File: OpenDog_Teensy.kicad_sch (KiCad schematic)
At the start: 62 parts

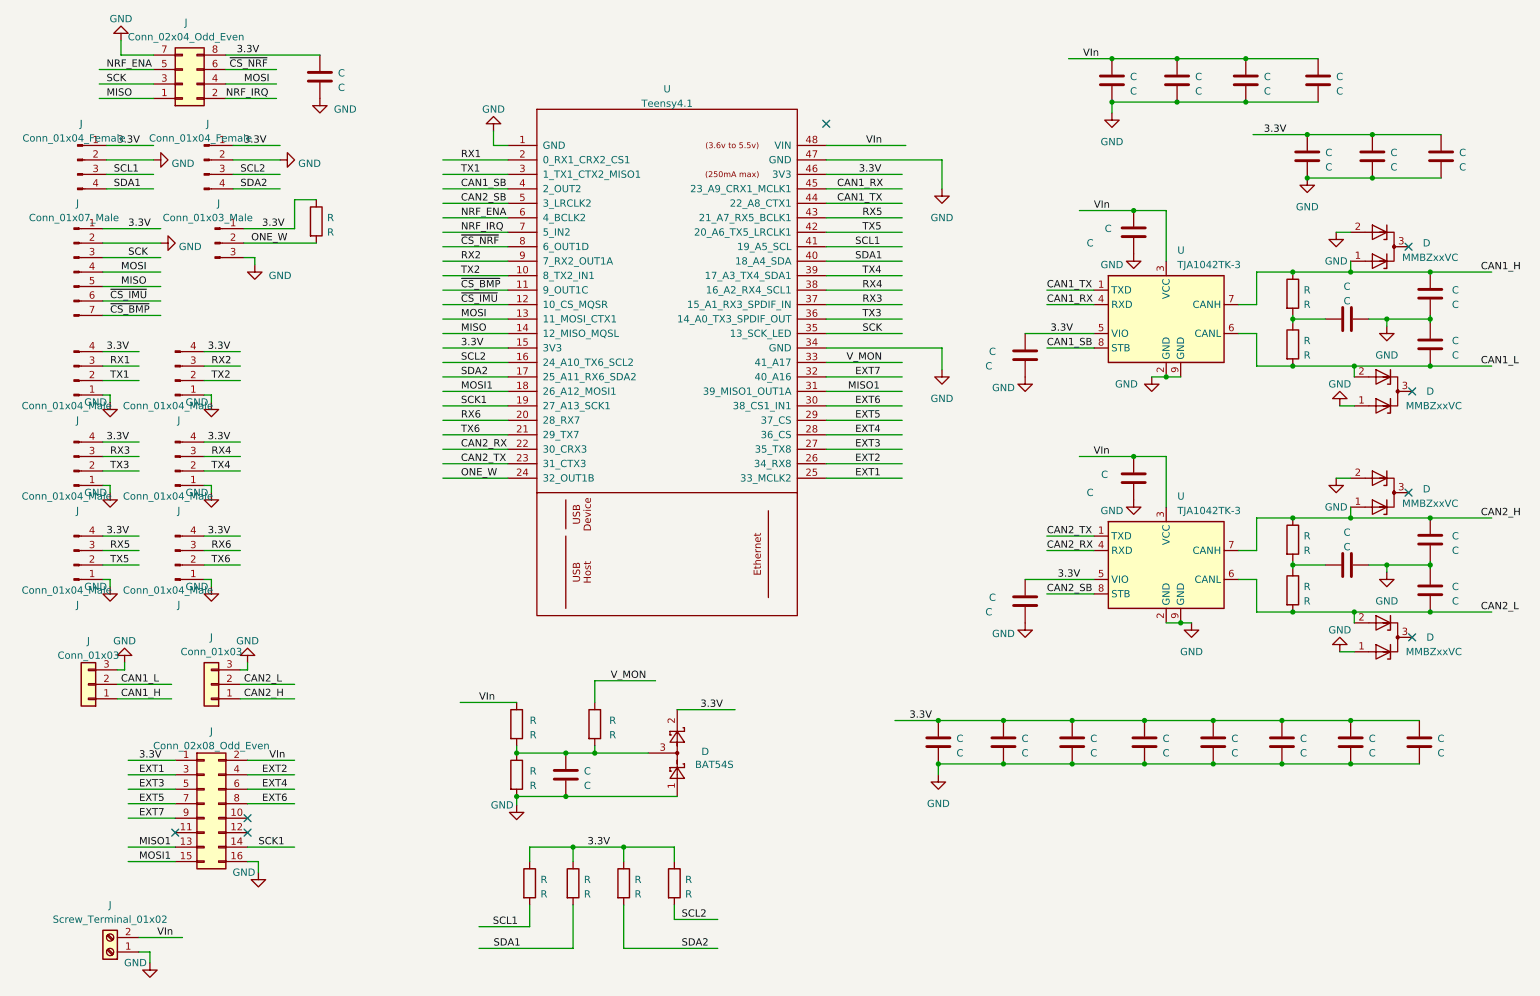
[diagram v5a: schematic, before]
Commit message: OpenDog_Teensy - add buck converter socket. Move the battery monitor to the battery input instead of the 5V input in the old version.
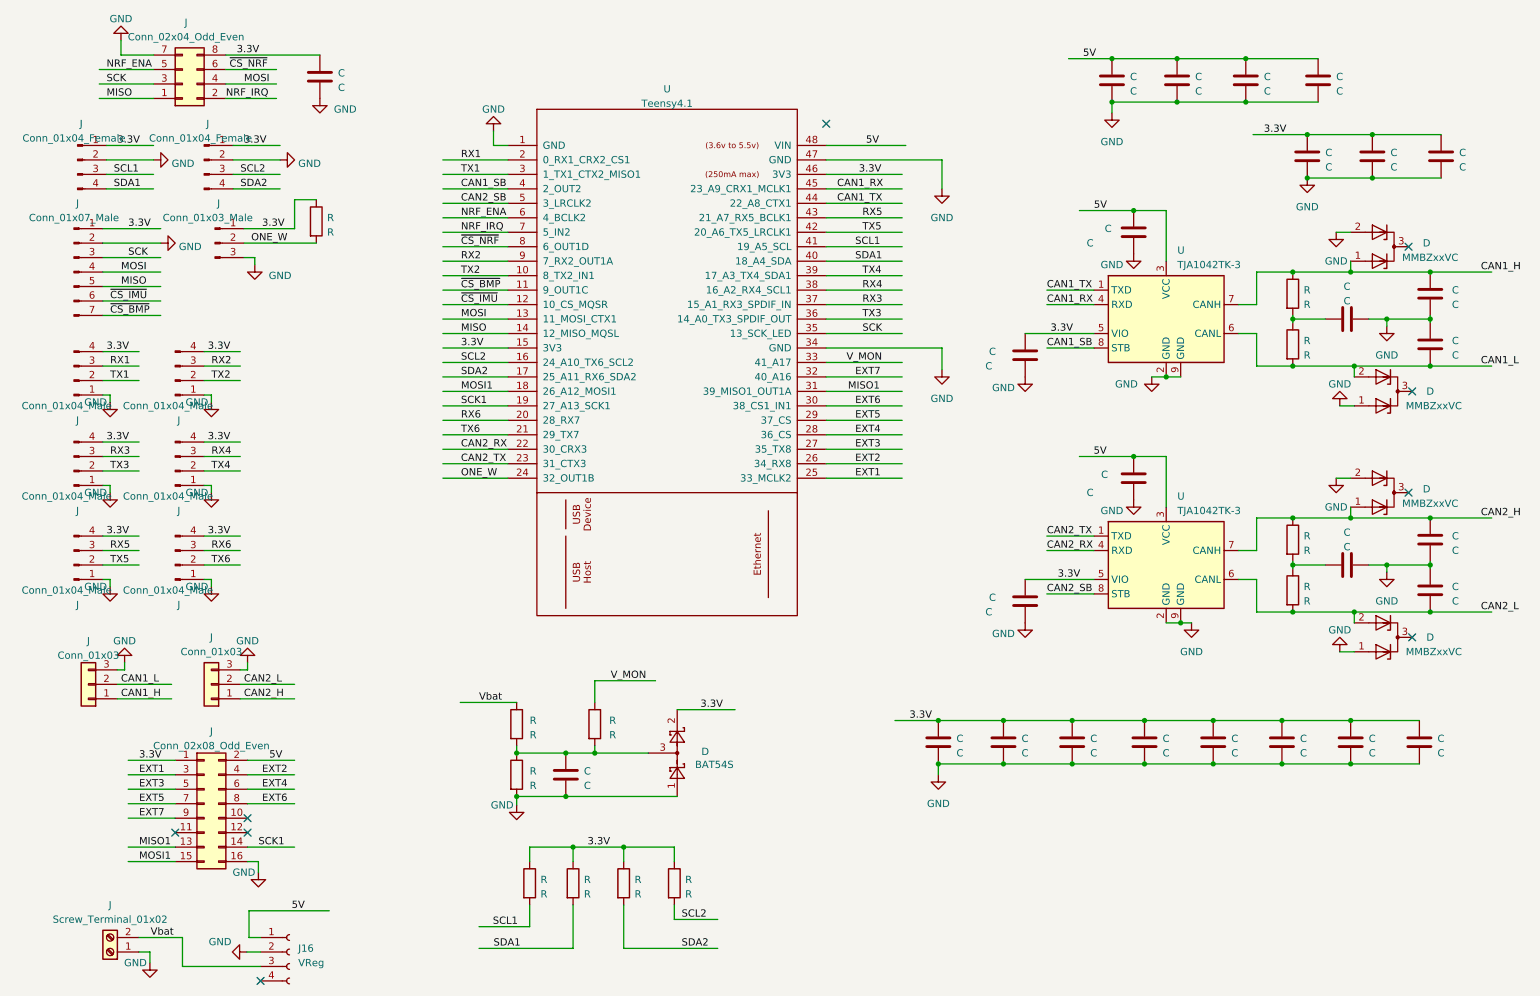
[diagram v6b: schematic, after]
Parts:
- added J16: VReg, Connector_PinSocket_2.54mm:PinSocket_1x04_P2.54mm_Vertical, symbol Connector:Conn_01x04_Female
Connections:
- net GND: now also J16.2 (Pin_2)
- net VIn renamed 5V
- net 5V: now also J16.1 (Pin_1); no longer J.2 (Pin_2), R.1
- new net Vbat: J.2 (Pin_2), J16.3 (Pin_3), R.1
- no-connect marks 8 -> 9
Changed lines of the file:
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@@
-(kicad_sch (version 20220404) (generator eeschema)
+(kicad_sch (version 20220820) (generator eeschema)
   (paper "A4")
   (junction (at 238.125 107.315) (diameter 0) (color 0 0 0 0)
@@
   (no_connect (at 54.61 160.02))
   (no_connect (at 156.21 38.1))
+  (no_connect (at 56.896 188.595))
   (wire (pts (xy 46.99 113.03) (xy 53.34 113.03))
     (stroke (width 0) (type default))
@@
     (stroke (width 0) (type default))
   )
+  (wire (pts (xy 43.18 186.055) (xy 43.18 180.975))
+    (stroke (width 0) (type default))
+  )
   (wire (pts (xy 95.25 182.88) (xy 111.76 182.88))
     (stroke (width 0) (type default))
@@
     (stroke (width 0) (type default))
   )
+  (wire (pts (xy 56.896 180.975) (xy 54.864 180.975))
+    (stroke (width 0) (type default))
+  )
   (wire (pts (xy 50.8 28.575) (xy 59.69 28.575))
     (stroke (width 0) (type default))
@@
     (stroke (width 0) (type default))
   )
+  (wire (pts (xy 56.896 186.055) (xy 43.18 186.055))
+    (stroke (width 0) (type default))
+  )
   (wire (pts (xy 88.9 80.01) (xy 100.33 80.01))
     (stroke (width 0) (type default))
@@
     (stroke (width 0) (type default))
   )
+  (wire (pts (xy 54.864 176.276) (xy 68.961 176.276))
+    (stroke (width 0) (type default))
+  )
   (wire (pts (xy 175.895 150.495) (xy 187.325 150.495))
     (stroke (width 0) (type default))
@@
     (stroke (width 0) (type default))
   )
+  (wire (pts (xy 54.864 180.975) (xy 54.864 176.276))
+    (stroke (width 0) (type default))
+  )
   (wire (pts (xy 129.54 165.1) (xy 120.65 165.1))
     (stroke (width 0) (type default))
@@
     (stroke (width 0) (type default))
   )
+  (wire (pts (xy 54.483 183.515) (xy 56.896 183.515))
+    (stroke (width 0) (type default))
+  )
   (wire (pts (xy 156.21 82.55) (xy 169.545 82.55))
     (stroke (width 0) (type default))
@@
     (effects (font (size 1.27 1.27)) (justify left bottom))
   )
-  (label "VIn" (at 203.2 53.34 0) (fields_autoplaced)
+  (label "5V" (at 203.2 53.34 0) (fields_autoplaced)
     (effects (font (size 1.27 1.27)) (justify left bottom))
   )
@@
     (effects (font (size 1.27 1.27)) (justify left bottom))
   )
-  (label "VIn" (at 203.1515 96.52 0) (fields_autoplaced)
+  (label "5V" (at 203.1515 96.52 0) (fields_autoplaced)
     (effects (font (size 1.27 1.27)) (justify left bottom))
   )
@@
     (effects (font (size 1.27 1.27)) (justify left bottom))
   )
-  (label "VIn" (at 163.195 41.91 0) (fields_autoplaced)
+  (label "5V" (at 163.195 41.91 0) (fields_autoplaced)
     (effects (font (size 1.27 1.27)) (justify left bottom))
   )
@@
     (effects (font (size 1.27 1.27)) (justify left bottom))
   )
+  (label "Vbat" (at 37.592 180.975 0) (fields_autoplaced)
+    (effects (font (size 1.27 1.27)) (justify left bottom))
+  )
   (label "SCL2" (at 53.34 46.99 0) (fields_autoplaced)
     (effects (font (size 1.27 1.27)) (justify left bottom))
@@
     (effects (font (size 1.27 1.27)) (justify left bottom))
   )
-  (label "VIn" (at 38.735 180.975 0) (fields_autoplaced)
-    (effects (font (size 1.27 1.27)) (justify left bottom))
-  )
   (label "TX1" (at 30.48 83.185 0) (fields_autoplaced)
     (effects (font (size 1.27 1.27)) (justify left bottom))
@@
     (effects (font (size 1.27 1.27)) (justify left bottom))
   )
+  (label "5V" (at 62.357 176.276 0) (fields_autoplaced)
+    (effects (font (size 1.27 1.27)) (justify left bottom))
+  )
   (label "CAN1_H" (at 32.385 139.065 0) (fields_autoplaced)
     (effects (font (size 1.27 1.27)) (justify left bottom))
@@
     (effects (font (size 1.27 1.27)) (justify left bottom))
   )
-  (label "VIn" (at 95.25 139.7 0) (fields_autoplaced)
+  (label "Vbat" (at 95.25 139.7 0) (fields_autoplaced)
     (effects (font (size 1.27 1.27)) (justify left bottom))
   )
@@
     (effects (font (size 1.27 1.27)) (justify left bottom))
   )
-  (label "VIn" (at 201.295 26.67 0) (fields_autoplaced)
+  (label "5V" (at 201.295 26.67 0) (fields_autoplaced)
     (effects (font (size 1.27 1.27)) (justify left bottom))
   )
@@
     (effects (font (size 1.27 1.27)) (justify left bottom))
   )
-  (label "VIn" (at 58.42 149.86 0) (fields_autoplaced)
+  (label "5V" (at 58.42 149.86 0) (fields_autoplaced)
     (effects (font (size 1.27 1.27)) (justify left bottom))
   )
@@
     (pin "3")
   )
+  (symbol (lib_id "power:GND") (at 54.483 183.515 270) (unit 1)
+    (in_bom yes) (on_board yes)
+    (default_instance (reference "#PWR") (unit 1) (value "GND") (footprint ""))
+    (property "Reference" "#PWR" (id 0) (at 48.133 183.515 0)
+      (effects (font (size 1.27 1.27)) hide)
+    )
+    (property "Value" "GND" (id 1) (at 49.784 181.737 90)
+      (effects (font (size 1.27 1.27)))
+    )
+    (property "Footprint" "" (id 2) (at 54.483 183.515 0)
+      (effects (font (size 1.27 1.27)) hide)
+    )
+    (property "Datasheet" "" (id 3) (at 54.483 183.515 0)
+      (effects (font (size 1.27 1.27)) hide)
+    )
+    (pin "1")
+  )
   (symbol (lib_id "power:GND") (at 48.26 86.995 0) (unit 1)
     (in_bom yes) (on_board yes)
@@
     (pin "2")
   )
+  (symbol (lib_id "Connector:Conn_01x04_Female") (at 61.976 183.515 0) (unit 1)
+    (in_bom yes) (on_board yes) (fields_autoplaced)
+    (default_instance (reference "J16") (unit 1) (value "VReg") (footprint "Connector_PinSocket_2.54mm:PinSocket_1x04_P2.54mm_Vertical"))
+    (property "Reference" "J16" (id 0) (at 63.5 182.88 0)
+      (effects (font (size 1.27 1.27)) (justify left))
+    )
+    (property "Value" "VReg" (id 1) (at 63.5 185.42 0)
+      (effects (font (size 1.27 1.27)) (justify left))
+    )
+    (property "Footprint" "Connector_PinSocket_2.54mm:PinSocket_1x04_P2.54mm_Vertical" (id 2) (at 61.976 183.515 0)
+      (effects (font (size 1.27 1.27)) hide)
+    )
+    (property "Datasheet" "~" (id 3) (at 61.976 183.515 0)
+      (effects (font (size 1.27 1.27)) hide)
+    )
+    (property "JLC Part #" "C2718488" (id 4) (at 61.976 183.515 0)
+      (effects (font (size 1.27 1.27)) hide)
+    )
+    (pin "1")
+    (pin "2")
+    (pin "3")
+    (pin "4")
+  )
   (symbol (lib_id "Connector:Conn_01x04_Male") (at 41.91 83.185 0) (mirror x) (unit 1)
     (in_bom yes) (on_board yes)
@@
       (reference "#PWR0129") (unit 1) (value "GND") (footprint "")
     )
+    (path "/43ae1265-c08d-4918-8c02-5519d0be2e44"
+      (reference "#PWR0130") (unit 1) (value "GND") (footprint "")
+    )
     (path "/aafc1360-2840-4378-8ce4-48f6f5898fa6"
       (reference "#PWR0130") (unit 1) (value "GND") (footprint "")
@@
       (reference "J15") (unit 1) (value "Power") (footprint "Connector_Phoenix_MSTB:PhoenixContact_MSTBA_2,5_2-G_1x02_P5.00mm_Horizontal")
     )
+    (path "/986a4f5c-c29e-4fea-a55b-2a37af8da8dc"
+      (reference "J16") (unit 1) (value "VReg") (footprint "Connector_PinSocket_2.54mm:PinSocket_1x04_P2.54mm_Vertical")
+    )
     (path "/f20f5656-102e-41f9-ba3f-0e35d3dd3685"

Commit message: OpenDog_Teensy - Update routing. Sent to fab.
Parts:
- R: JLC Part # C23162 -> C23254
- R: JLC Part # C4190 -> C31850
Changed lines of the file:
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@@
       (effects (font (size 1.27 1.27)) hide)
     )
-    (property "JLC Part #" "C23162" (id 4) (at 101.854 143.51 0)
+    (property "JLC Part #" "C23254" (id 4) (at 101.854 143.51 0)
       (effects (font (size 1.27 1.27)) hide)
     )
@@
       (effects (font (size 1.27 1.27)) hide)
     )
-    (property "JLC Part #" "C4190" (id 4) (at 101.854 152.4 0)
+    (property "JLC Part #" "C31850" (id 4) (at 101.854 152.4 0)
       (effects (font (size 1.27 1.27)) hide)
     )
@@
       (reference "#PWR0129") (unit 1) (value "GND") (footprint "")
     )
-    (path "/43ae1265-c08d-4918-8c02-5519d0be2e44"
-      (reference "#PWR0130") (unit 1) (value "GND") (footprint "")
-    )
     (path "/aafc1360-2840-4378-8ce4-48f6f5898fa6"
       (reference "#PWR0130") (unit 1) (value "GND") (footprint "")
@@
       (reference "#PWR0132") (unit 1) (value "GND") (footprint "")
     )
+    (path "/43ae1265-c08d-4918-8c02-5519d0be2e44"
+      (reference "#PWR0133") (unit 1) (value "GND") (footprint "")
+    )
     (path "/f786820a-c169-498f-ab00-951d998b096a"
       (reference "C1") (unit 1) (value "100nF") (footprint "Capacitor_SMD:C_0603_1608Metric")
@@
     )
     (path "/3e60e271-a6ba-4e4b-bcd7-ceef2391dbae"
-      (reference "R6") (unit 1) (value "4.7k") (footprint "Resistor_SMD:R_0603_1608Metric")
+      (reference "R6") (unit 1) (value "82k") (footprint "Resistor_SMD:R_0603_1608Metric")
     )
     (path "/5f08a27d-840c-4511-bcc0-86da6dff80bc"
-      (reference "R7") (unit 1) (value "2.2k") (footprint "Resistor_SMD:R_0603_1608Metric")
+      (reference "R7") (unit 1) (value "22k") (footprint "Resistor_SMD:R_0603_1608Metric")
     )
     (path "/ad100dc4-8615-423e-8189-f8de466e7713"

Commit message: Add OpenDog Remote Board.
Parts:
- C1, C15, C16, C17, C18, C19, C2, C20, C21, C22, C23, C24, C25, C26, C27, C3, C4, C5, C6: renamed from C; value C -> 100nF; footprint (none) -> Capacitor_SMD:C_0603_1608Metric
- C10, C7: renamed from C; value C -> 4700pF; footprint (none) -> Capacitor_SMD:C_0603_1608Metric
- C11, C12, C8, C9: renamed from C; value C -> 47pF; footprint (none) -> Capacitor_SMD:C_0603_1608Metric
- C13, C14: renamed from C; value C -> 10nF; footprint (none) -> Capacitor_SMD:C_0603_1608Metric
- D1, D2, D3, D4: renamed from D; value MMBZxxVC -> MMBZ27VC
- J1: renamed from J; value Conn_02x04_Odd_Even -> NRF; footprint (none) -> Connector_PinSocket_2.54mm:PinSocket_2x04_P2.54mm_Vertical
- J10: renamed from J; value Conn_01x04_Male -> UART5; footprint (none) -> Connector_JST:JST_EH_S4B-EH_1x04_P2.50mm_Horizontal
- J11: renamed from J; value Conn_01x04_Male -> UART6; footprint (none) -> Connector_JST:JST_EH_S4B-EH_1x04_P2.50mm_Horizontal
- J12: renamed from J; value Conn_01x03 -> CAN1; footprint (none) -> Connector_JST:JST_EH_S3B-EH_1x03_P2.50mm_Horizontal
- J13: renamed from J; value Conn_01x03 -> CAN2; footprint (none) -> Connector_JST:JST_EH_S3B-EH_1x03_P2.50mm_Horizontal
- J14: renamed from J; value Conn_02x08_Odd_Even -> EXP; footprint (none) -> Connector_PinSocket_2.54mm:PinSocket_2x08_P2.54mm_Vertical
- J15: renamed from J; value Screw_Terminal_01x02 -> Power; footprint (none) -> Connector_Phoenix_MSTB:PhoenixContact_MSTBA_2,5_2-G_1x02_P5.00mm_Horizontal
- J2: renamed from J; value Conn_01x04_Female -> TOF1; footprint (none) -> Connector_JST:JST_EH_S4B-EH_1x04_P2.50mm_Horizontal
- J3: renamed from J; value Conn_01x04_Female -> TOF2; footprint (none) -> Connector_JST:JST_EH_S4B-EH_1x04_P2.50mm_Horizontal
- J4: renamed from J; value Conn_01x07_Male -> IMU; footprint (none) -> Connector_JST:JST_EH_S7B-EH_1x07_P2.50mm_Horizontal
- J5: renamed from J; value Conn_01x03_Male -> One W; footprint (none) -> Connector_JST:JST_EH_S3B-EH_1x03_P2.50mm_Horizontal
- J6: renamed from J; value Conn_01x04_Male -> UART1; footprint (none) -> Connector_JST:JST_EH_S4B-EH_1x04_P2.50mm_Horizontal
- J7: renamed from J; value Conn_01x04_Male -> UART2; footprint (none) -> Connector_JST:JST_EH_S4B-EH_1x04_P2.50mm_Horizontal
- J8: renamed from J; value Conn_01x04_Male -> UART3; footprint (none) -> Connector_JST:JST_EH_S4B-EH_1x04_P2.50mm_Horizontal
- J9: renamed from J; value Conn_01x04_Male -> UART4; footprint (none) -> Connector_JST:JST_EH_S4B-EH_1x04_P2.50mm_Horizontal
- R1, R2, R3, R4: renamed from R; value R -> 60.4; footprint (none) -> Resistor_SMD:R_0603_1608Metric
- R10, R11, R12, R5, R9: renamed from R; value R -> 1k; footprint (none) -> Resistor_SMD:R_0603_1608Metric
- R6: renamed from R; value R -> 82k; footprint (none) -> Resistor_SMD:R_0603_1608Metric
- R7: renamed from R; value R -> 22k; footprint (none) -> Resistor_SMD:R_0603_1608Metric
- R8: renamed from R; value R -> 10k; footprint (none) -> Resistor_SMD:R_0603_1608Metric
- U1: renamed from U; footprint (none) -> Teensy:Teensy41-Simple
- renumbered D to D5, U to U2, U to U3
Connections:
- no-connect marks 9 -> 8
